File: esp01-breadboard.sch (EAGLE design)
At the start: 7 parts

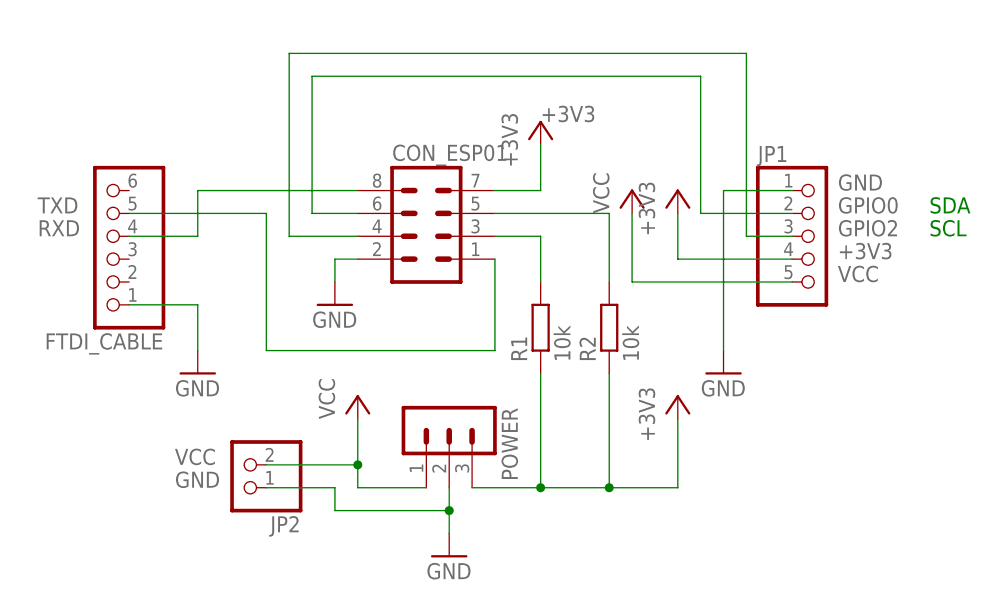
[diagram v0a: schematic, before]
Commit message: Added reset button
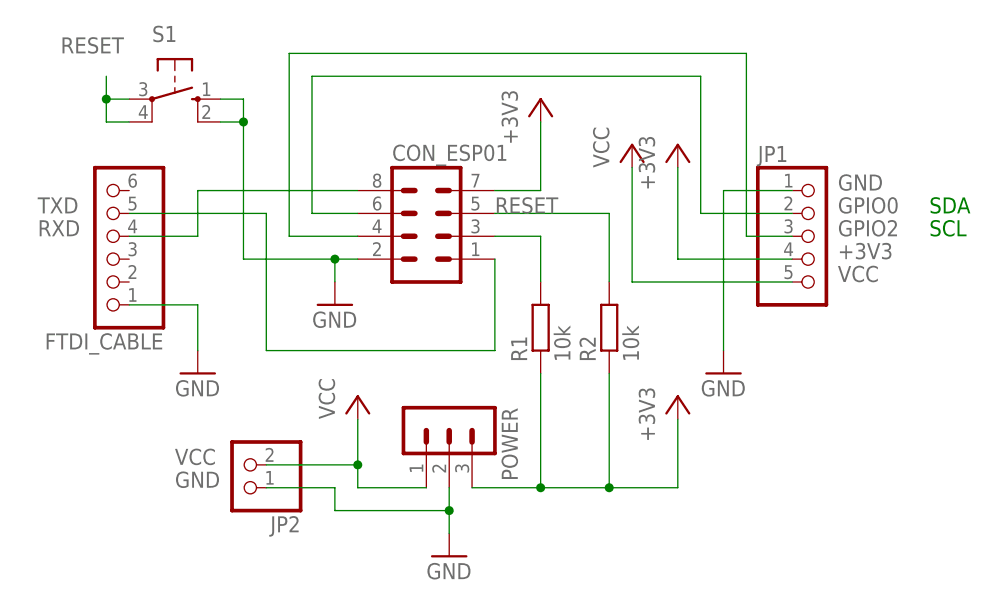
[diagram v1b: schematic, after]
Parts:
- added S1: (no value), switch-omron:10-XX
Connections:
- removed net N$2: CON_ESP01.5, R2.2
- new net RESET: CON_ESP01.5, R2.2, S1.P, S1.P1
- net GND: now also S1.S, S1.S1
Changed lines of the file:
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@@
 <part name="+3V3" library="supply1" deviceset="+3V3" device=""/>
 <part name="JP2" library="pinhead" deviceset="PINHD-1X2" device=""/>
+<part name="S1" library="switch-omron" deviceset="10-XX" device=""/>
 </parts>
 <sheets>
@@
 <instance part="P+1" gate="VCC" x="157.48" y="30.48"/>
 <instance part="+3V1" gate="G$1" x="193.04" y="30.48"/>
-<instance part="+3V2" gate="G$1" x="177.8" y="60.96"/>
+<instance part="+3V2" gate="G$1" x="177.8" y="63.5"/>
 <instance part="FTDI_CABLE" gate="A" x="129.54" y="48.26" rot="R180"/>
 <instance part="GND4" gate="1" x="139.7" y="33.02"/>
 <instance part="R1" gate="G$1" x="177.8" y="38.1" rot="R90"/>
 <instance part="R2" gate="G$1" x="185.42" y="38.1" rot="R90"/>
-<instance part="P+2" gate="VCC" x="187.96" y="53.34"/>
-<instance part="+3V3" gate="G$1" x="193.04" y="53.34"/>
+<instance part="P+2" gate="VCC" x="187.96" y="58.42"/>
+<instance part="+3V3" gate="G$1" x="193.04" y="58.42"/>
 <instance part="JP2" gate="G$1" x="144.78" y="22.86" rot="R180"/>
+<instance part="S1" gate="1" x="137.16" y="63.5" rot="R270"/>
 </instances>
 <busses>
@@
 <pinref part="CON_ESP01" gate="G$1" pin="2"/>
 <wire x1="154.94" y1="45.72" x2="157.48" y2="45.72" width="0.1524" layer="91"/>
+<pinref part="S1" gate="1" pin="S"/>
+<wire x1="142.24" y1="63.5" x2="144.78" y2="63.5" width="0.1524" layer="91"/>
+<wire x1="144.78" y1="63.5" x2="144.78" y2="60.96" width="0.1524" layer="91"/>
+<wire x1="144.78" y1="60.96" x2="144.78" y2="45.72" width="0.1524" layer="91"/>
+<wire x1="144.78" y1="45.72" x2="154.94" y2="45.72" width="0.1524" layer="91"/>
+<junction x="154.94" y="45.72"/>
+<pinref part="S1" gate="1" pin="S1"/>
+<wire x1="142.24" y1="60.96" x2="144.78" y2="60.96" width="0.1524" layer="91"/>
+<junction x="144.78" y="60.96"/>
 </segment>
 <segment>
@@
 <pinref part="P+2" gate="VCC" pin="VCC"/>
 <wire x1="205.74" y1="43.18" x2="187.96" y2="43.18" width="0.1524" layer="91"/>
-<wire x1="187.96" y1="43.18" x2="187.96" y2="50.8" width="0.1524" layer="91"/>
+<wire x1="187.96" y1="43.18" x2="187.96" y2="55.88" width="0.1524" layer="91"/>
 <label x="210.82" y="43.18" size="1.778" layer="95"/>
 </segment>
@@
 <pinref part="+3V2" gate="G$1" pin="+3V3"/>
 <wire x1="172.72" y1="53.34" x2="177.8" y2="53.34" width="0.1524" layer="91"/>
-<wire x1="177.8" y1="53.34" x2="177.8" y2="58.42" width="0.1524" layer="91"/>
-<label x="177.8" y="60.96" size="1.778" layer="95"/>
+<wire x1="177.8" y1="53.34" x2="177.8" y2="60.96" width="0.1524" layer="91"/>
 </segment>
 <segment>
@@
 <pinref part="+3V3" gate="G$1" pin="+3V3"/>
 <wire x1="205.74" y1="45.72" x2="193.04" y2="45.72" width="0.1524" layer="91"/>
-<wire x1="193.04" y1="45.72" x2="193.04" y2="50.8" width="0.1524" layer="91"/>
+<wire x1="193.04" y1="45.72" x2="193.04" y2="55.88" width="0.1524" layer="91"/>
 <label x="210.82" y="45.72" size="1.778" layer="95"/>
 </segment>
@@
 </segment>
 </net>
-<net name="N$2" class="0">
+<net name="RESET" class="0">
 <segment>
 <pinref part="CON_ESP01" gate="G$1" pin="5"/>
@@
 <wire x1="172.72" y1="50.8" x2="185.42" y2="50.8" width="0.1524" layer="91"/>
 <wire x1="185.42" y1="50.8" x2="185.42" y2="43.18" width="0.1524" layer="91"/>
+<label x="172.72" y="50.8" size="1.778" layer="95"/>
+</segment>
+<segment>
+<pinref part="S1" gate="1" pin="P1"/>
+<wire x1="132.08" y1="60.96" x2="129.54" y2="60.96" width="0.1524" layer="91"/>
+<wire x1="129.54" y1="60.96" x2="129.54" y2="63.5" width="0.1524" layer="91"/>
+<pinref part="S1" gate="1" pin="P"/>
+<wire x1="129.54" y1="63.5" x2="129.54" y2="66.04" width="0.1524" layer="91"/>
+<wire x1="132.08" y1="63.5" x2="129.54" y2="63.5" width="0.1524" layer="91"/>
+<junction x="129.54" y="63.5"/>
+<label x="124.46" y="68.58" size="1.778" layer="95"/>
 </segment>
 </net>
